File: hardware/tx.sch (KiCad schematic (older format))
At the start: 63 parts, among them Q1 RE1C002UN, U1 ADF4158, U10 HMC431LP4, U12 PAT1220-6dB, U15 SMA, U17 SE5004L, U3 PAT1220-6dB, U7 TLV172DCK

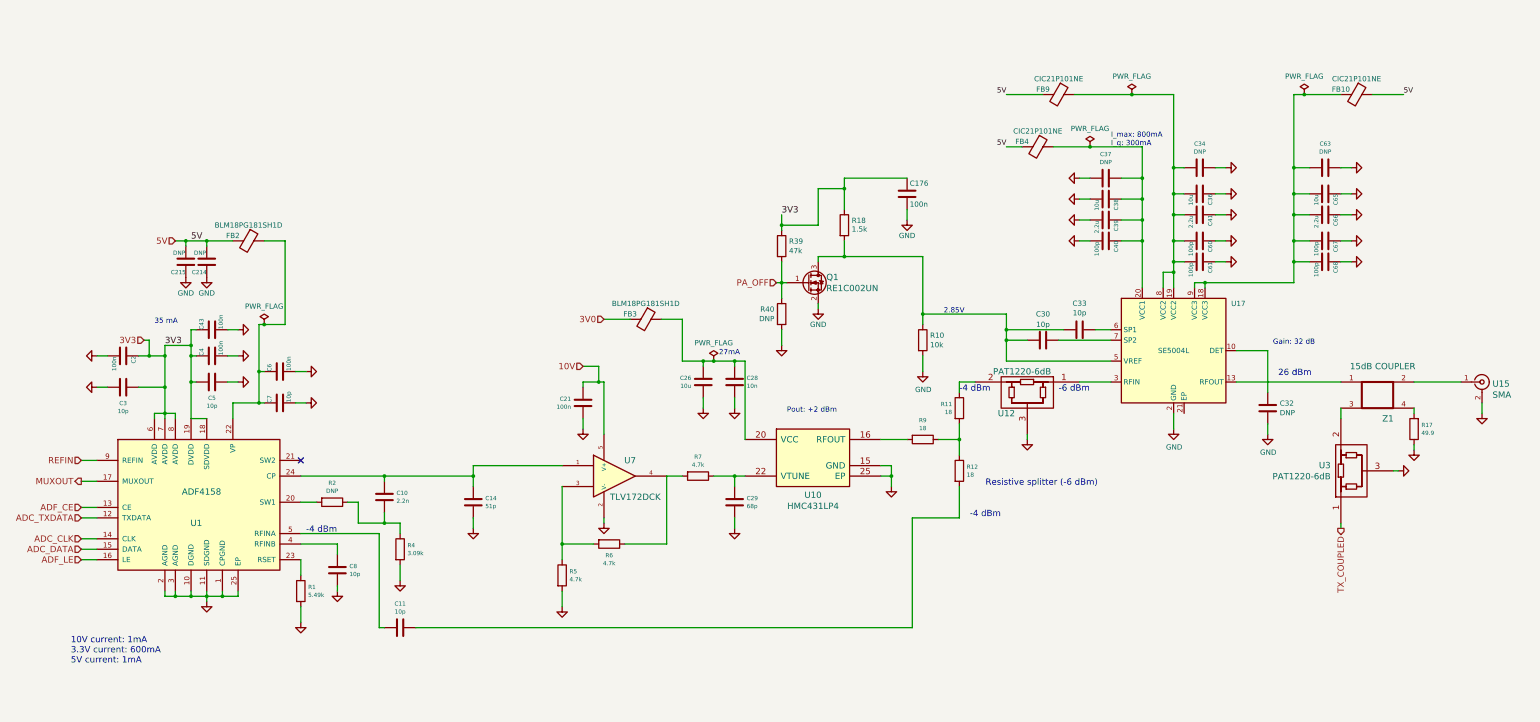
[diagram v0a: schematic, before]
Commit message: Improved tx sheet and corresponding documentation.
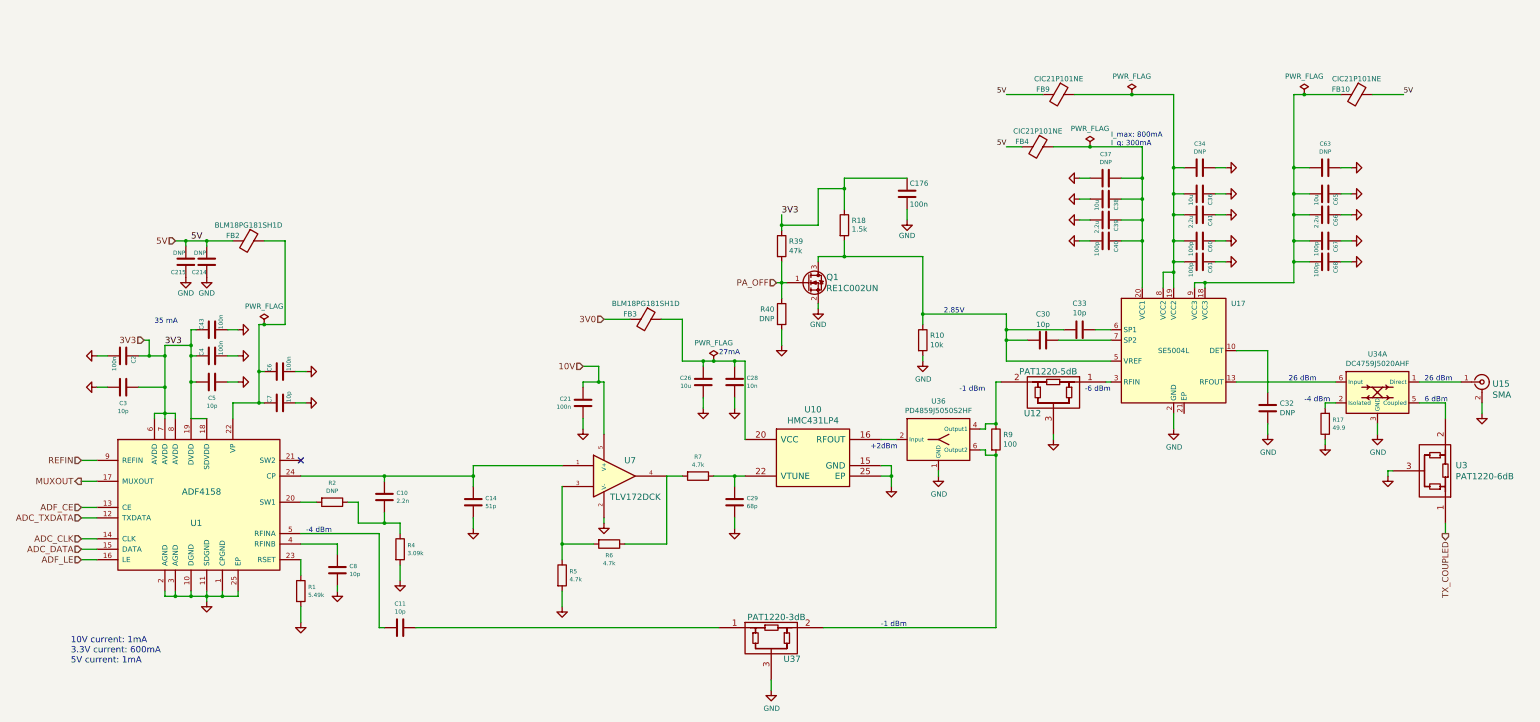
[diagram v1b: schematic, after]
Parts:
- removed R11, R12: 18, Resistor_SMD:R_0402_1005Metric, symbol Device:R
- removed Z1: 15dB COUPLER, fmcw:coupler, symbol fmcw-rescue:BRANCHLINE-fmcw3-rescue
- added U34: DC4759J5020AHF, RF_Converter:Anaren_Coupler_DC4759J5020AHF, symbol RF:DC4759J5020AHF
- added U36: PD4859J5050S2HF, RF_Converter:Anaren_0805_2012Metric-6, symbol RF:PD4859J5050S2HF
- added U37: PAT1220-3dB, fmcw:PAT1220, symbol fmcw-rescue:PAT1220-fmcw3-rescue
- R9: value 18 -> 100; footprint Resistor_SMD:R_0402_1005Metric -> Resistor_SMD:R_0603_1608Metric; MFN ERJ-2RKF18R0X -> ERA-3AEB101V
- U12: value PAT1220-6dB -> PAT1220-5dB; MFN PAT1220-C-6DB-T5 -> PAT1220-C-5DB-T5
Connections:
- net GND: now also U34.3 (GND), U34.4 (GND), U36.1 (GND), U36.3 (GND), U36.5 (GND), U37.3
- net at U10.16 (RFOUT): now also U36.2 (Input); no longer R9.2
- net at U15.1 (In): now also U34.1 (Direct)
- net at R9.1: now also U12.2, U36.4 (Output1)
- net at C11.1: now also U37.1
- net at U3.2: now also U34.5 (Coupled)
- net at U17.13 (RFOUT): now also U34.6 (Input)
- net at R17.2: now also U34.2 (Isolated)
- new net: R9.2, U36.6 (Output2), U37.2
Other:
- note added: "+2dBm"
- note added: "-1 dBm"
- note added: "6 dBm"
- note removed: "Gain: 32 dB"
- note removed: "Pout: +2 dBm"
- note removed: "Resistive splitter (-6 dBm)"
- moved on the sheet: R17, U12, U3

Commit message: Improved documentation and parts of the schematic.
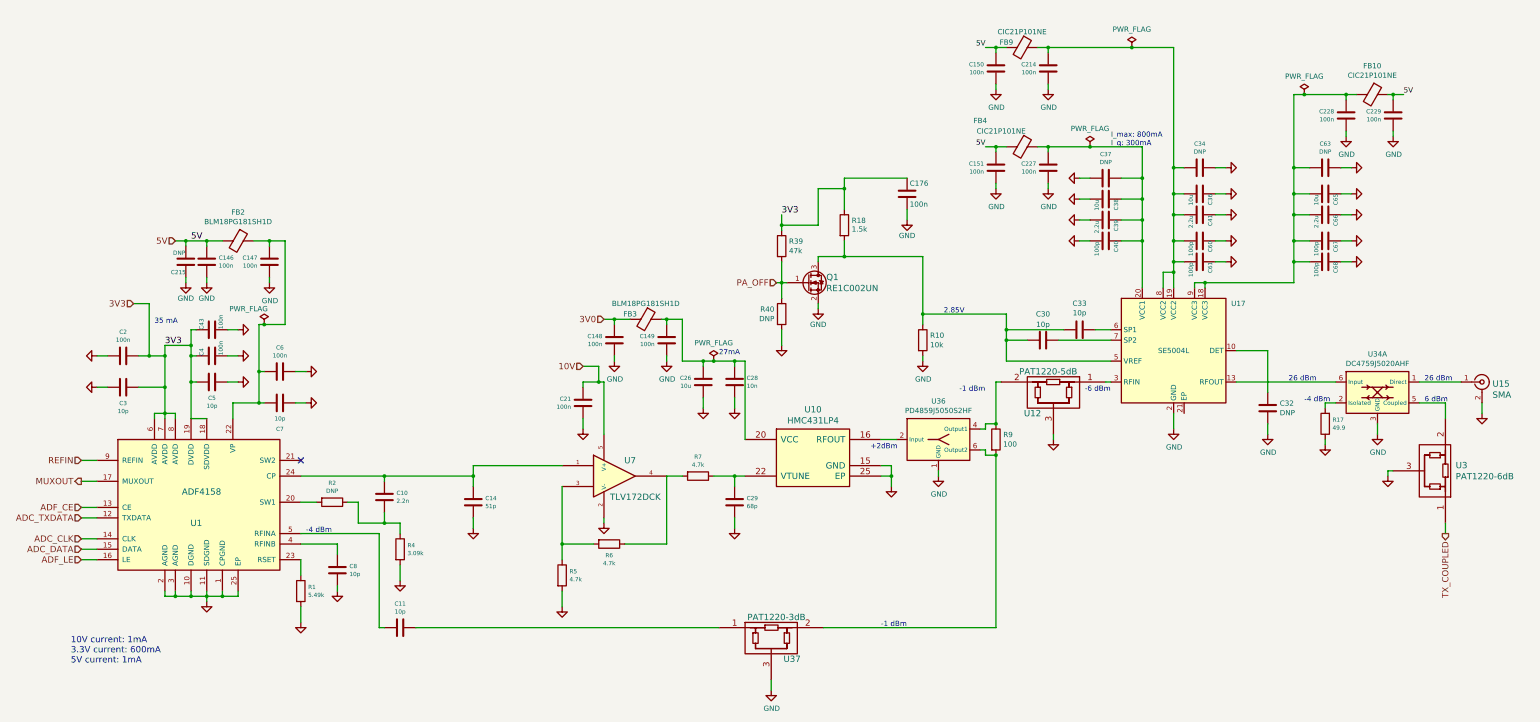
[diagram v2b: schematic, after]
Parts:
- added C146, C147, C148, C149, C150, C151, C227, C228, C229: 100n, Capacitor_SMD:C_0402_1005Metric, symbol Device:C
- C214: value DNP -> 100n; footprint Capacitor_SMD:C_0805_2012Metric -> Capacitor_SMD:C_0402_1005Metric; MFN (none) -> CL05B104KO5NNNC
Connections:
- net 3V0: now also C148.1
- net 5V: now also C146.1, C150.1, C151.1, C229.1; no longer C214.2
- net GND: now also C214.2, C146.2, C147.2, C148.2, C149.2, C150.2, C151.2, C227.2, C228.2, C229.2; no longer C214.1
- net at C26.1, C28.1, FB3.1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: now also C149.1
- net at C6.1, C7.1, FB2.1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: now also C147.1
- net at C37.1, C38.1, C39.1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: now also C227.1
- net at C63.2, C65.2, C66.2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: now also C228.1
- net at C34.2, C36.2, C41.2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: now also C214.1
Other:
- moved on the sheet: FB10, FB2, FB4, FB9

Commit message: Changed components to official libs.
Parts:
- removed C215: DNP, Capacitor_SMD:C_0805_2012Metric, symbol Device:C
- U1: footprint Package_DFN_QFN:WQFN-24-1EP_4x4mm_P0.5mm_EP2.7x2.7mm -> Package_CSP:LFCSP-24-1EP_4x4mm_P0.5mm_EP2.5x2.5mm; symbol fmcw-rescue:ADF4158-fmcw3-rescue -> Timer_PLL:ADF4158
- U10: footprint Package_DFN_QFN:VQFN-24-1EP_4x4mm_P0.5mm_EP2.45x2.45mm -> Package_DFN_QFN:QFN-24-1EP_4x4mm_P0.5mm_EP2.8x2.8mm; symbol fmcw-rescue:HMC431LP4-fmcw3-rescue -> RF:HMC431
- U12: footprint fmcw:PAT1220 -> RF_Converter:RF_Attenuator_Susumu_PAT1220; symbol fmcw-rescue:PAT1220-fmcw3-rescue -> RF:PAT1220x5DB
- U3: footprint fmcw:PAT1220 -> RF_Converter:RF_Attenuator_Susumu_PAT1220; symbol fmcw-rescue:PAT1220-fmcw3-rescue -> RF:PAT1220x6DB
- U37: footprint fmcw:PAT1220 -> RF_Converter:RF_Attenuator_Susumu_PAT1220; symbol fmcw-rescue:PAT1220-fmcw3-rescue -> RF:PAT1220x3DB
- U7: symbol fmcw-rescue:TLV172DCK-fmcw3-rescue -> Amplifier_Operational:TLV172IDCK
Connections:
- net GND: now also R4.1; no longer R4.2
- net at C10.2, R2.1: now also R4.2; no longer R4.1
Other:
- moved on the sheet: C10, C14, C146, C147, C2, C3, C4, C43, C5, C6, C7, C8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

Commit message: Finished design, began routing.
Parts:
- added C251, C252: 10p, Capacitor_SMD:C_0402_1005Metric, symbol Device:C
- C110: renamed from C10; MFN CL05B223KP5NNNC -> CL05B222KB5VPNC
- R40: renamed from R5; MFN ERJ-2GEJ472X -> ERJ-2GEJ472X
- R41: renamed from R6; MFN ERJ-2GEJ472X -> ERJ-2GEJ472X
- R42: renamed from R7; MFN ERJ-2GEJ472X -> ERJ-2GEJ472X
- U19: renamed from U34; footprint RF_Converter:Anaren_Coupler_DC4759J5020AHF -> RF_Converter:Anaren_0805_2012Metric-6; symbol RF:DC4759J5020AHF -> RF:DC4759J5020AHF-2
- renumbered C2 to C102, C3 to C103, C43 to C104, C4 to C105, C5 to C106, C8 to C107, C6 to C108, C7 to C109, C147 to C111, C11 to C112, C146 to C113, C14 to C114, C21 to C115, C148 to C116, C149 to C117, C26 to C118, C28 to C119, C29 to C120, C176 to C121, C150 to C122, C151 to C123, C30 to C124, C214 to C125, C227 to C126, C33 to C127, C37 to C128, C38 to C129, C39 to C130, C40 to C131, C34 to C132, C36 to C133, C41 to C134, C60 to C135, C61 to C136, C32 to C137, C63 to C138, C65 to C139, C66 to C140, C67 to C141, C68 to C142, C228 to C143, C229 to C144, FB2 to FB6, FB3 to FB7, FB9 to FB8, FB4 to FB9, U15 to J3, Q1 to Q2, R1 to R37, R2 to R38, R4 to R39, R39 to R43, R40 to R44, R18 to R45, R10 to R46, R9 to R47, R17 to R48, U1 to U12, U7 to U13, U37 to U14, U10 to U15, U36 to U16, U12 to U17, U17 to U18, U3 to U20
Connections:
- net at J3.1 (In): now also U19.6 (Direct); no longer U19.1 (Direct)
- net at U17.1: now also C251.2; no longer U18.3 (RFIN)
- net at U20.2: now also U19.2 (Coupled); no longer U19.5 (Coupled)
- net at R48.2: now also U19.5 (Isolated); no longer U19.2 (Isolated)
- net at U18.13 (RFOUT): now also C252.2; no longer U19.6 (Input)
- new net: C251.1, U18.3 (RFIN)
- new net: C252.1, U19.1 (Input)
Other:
- moved on the sheet: C122, C123, C125, C126, C128, C129, C130, C131, C132, C133, C134, C135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

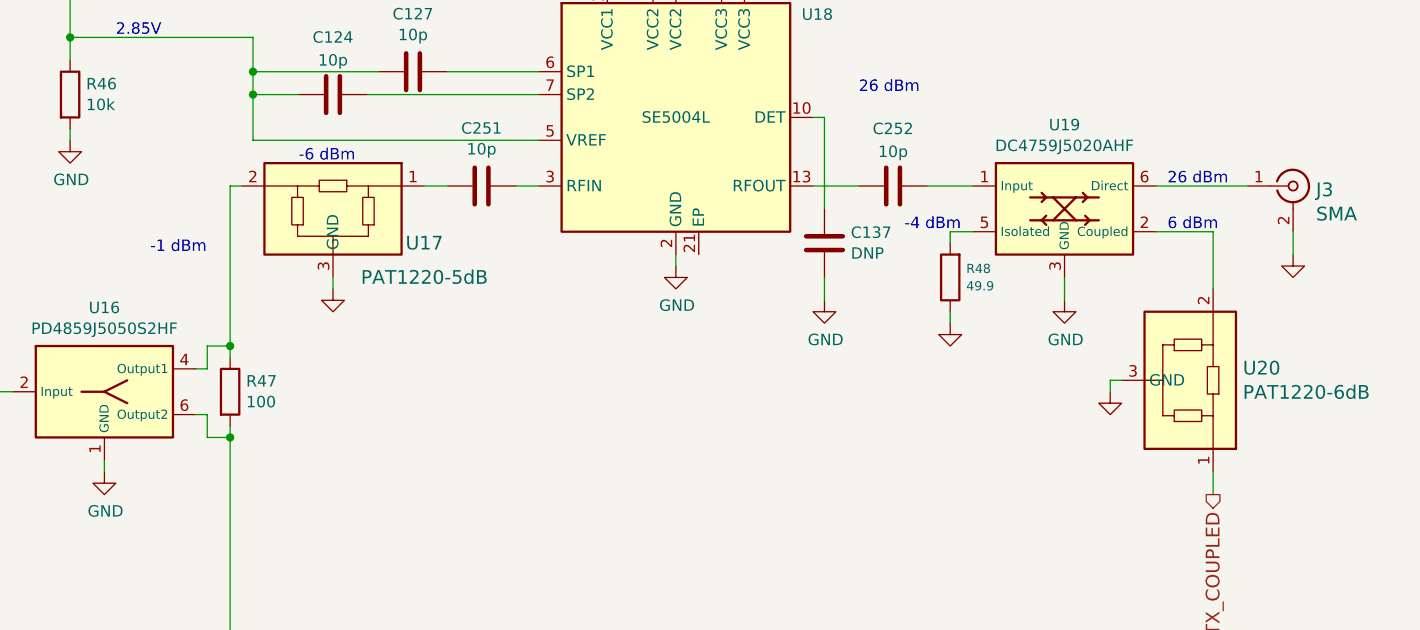
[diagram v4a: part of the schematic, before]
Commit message: Placed most major components.
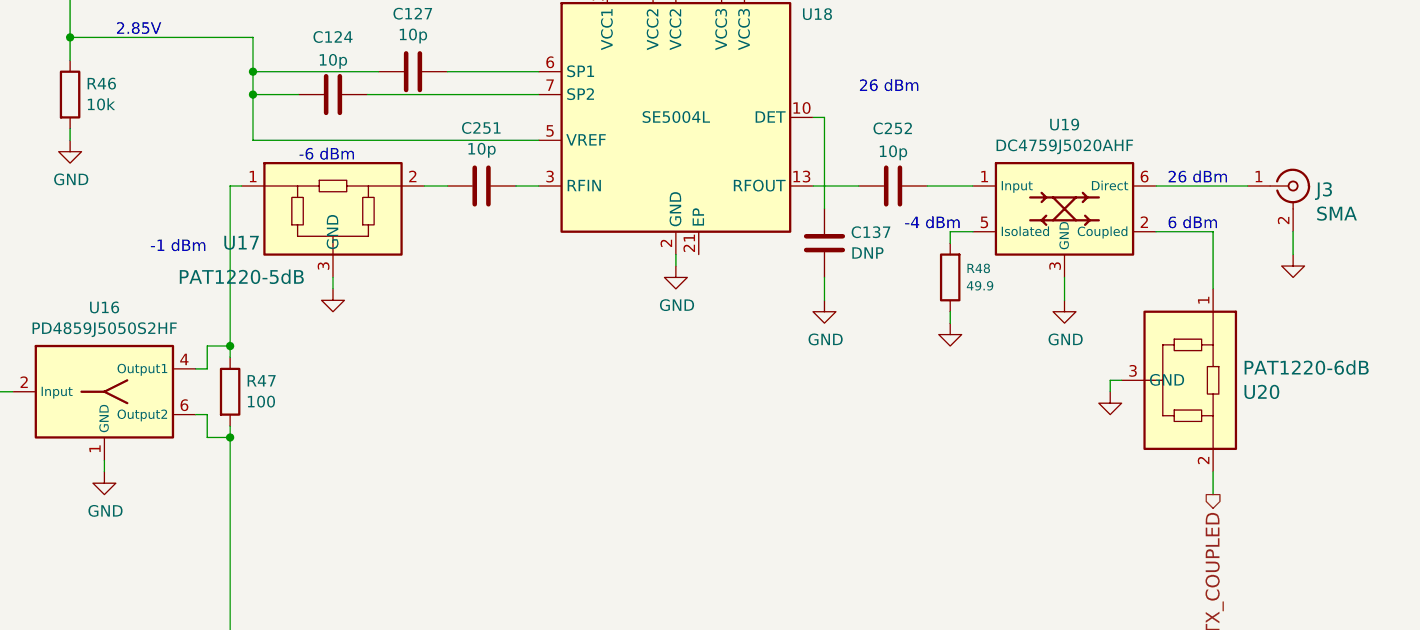
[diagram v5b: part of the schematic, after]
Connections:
- net TX_COUPLED: now also U20.2; no longer U20.1
- net at U17.1: now also R47.1, U16.4 (Output1); no longer C251.2
- net at U19.2 (Coupled): now also U20.1; no longer U20.2
- new net: C251.2, U17.2
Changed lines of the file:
@@
 F 4 "PAT1220-C-5DB-T5" H 150 100 50  0001 C CNN "MFN"
 	1    11350 5100
-	-1   0    0    -1
+	1    0    0    -1
 $EndComp
 $Comp
@@
 F 4 "PAT1220-C-6DB-T5" H 900 0   50  0001 C CNN "MFN"
 	1    15100 5850
-	0    1    -1   0
-$EndComp
-$Comp
+	0    1    1    0
+$EndComp
+$Comp

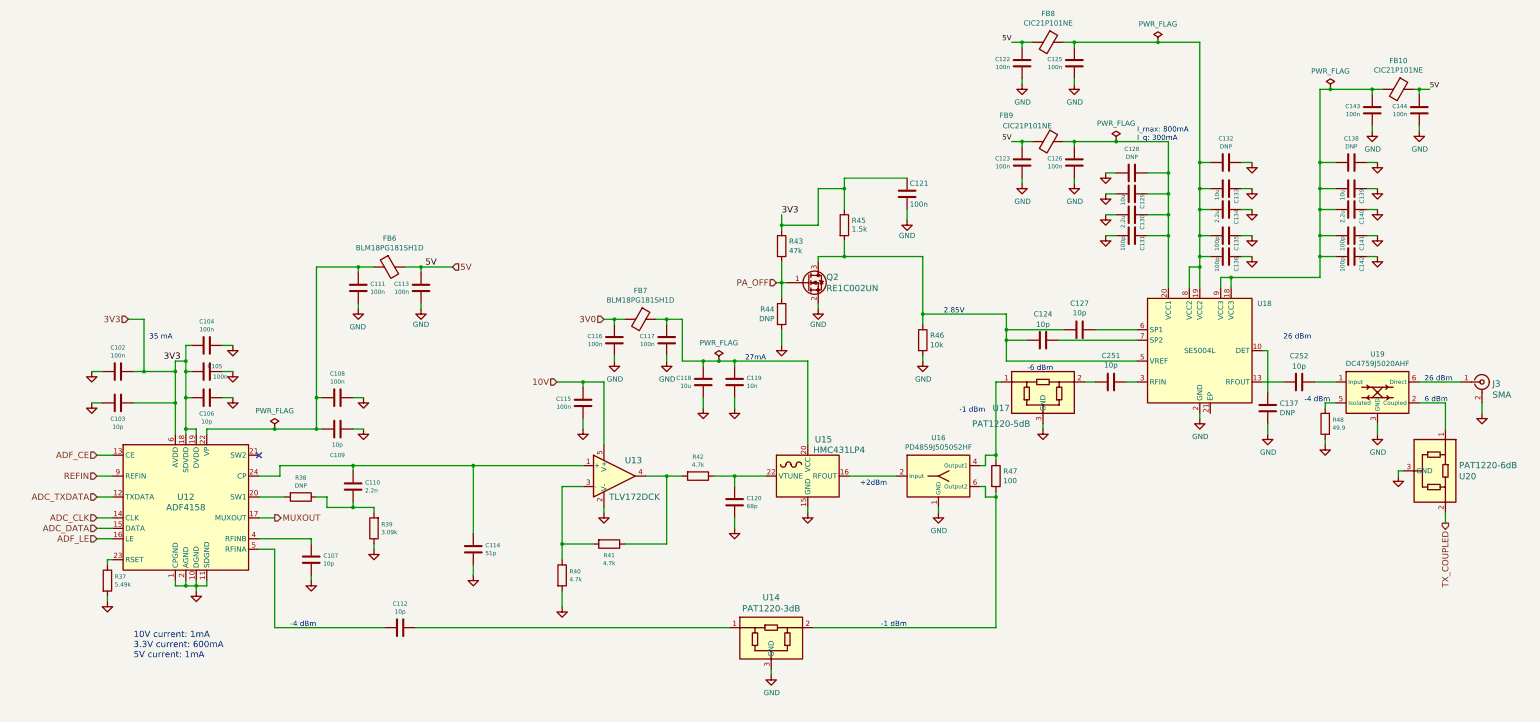
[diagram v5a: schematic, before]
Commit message: Completed clock placement and routing.
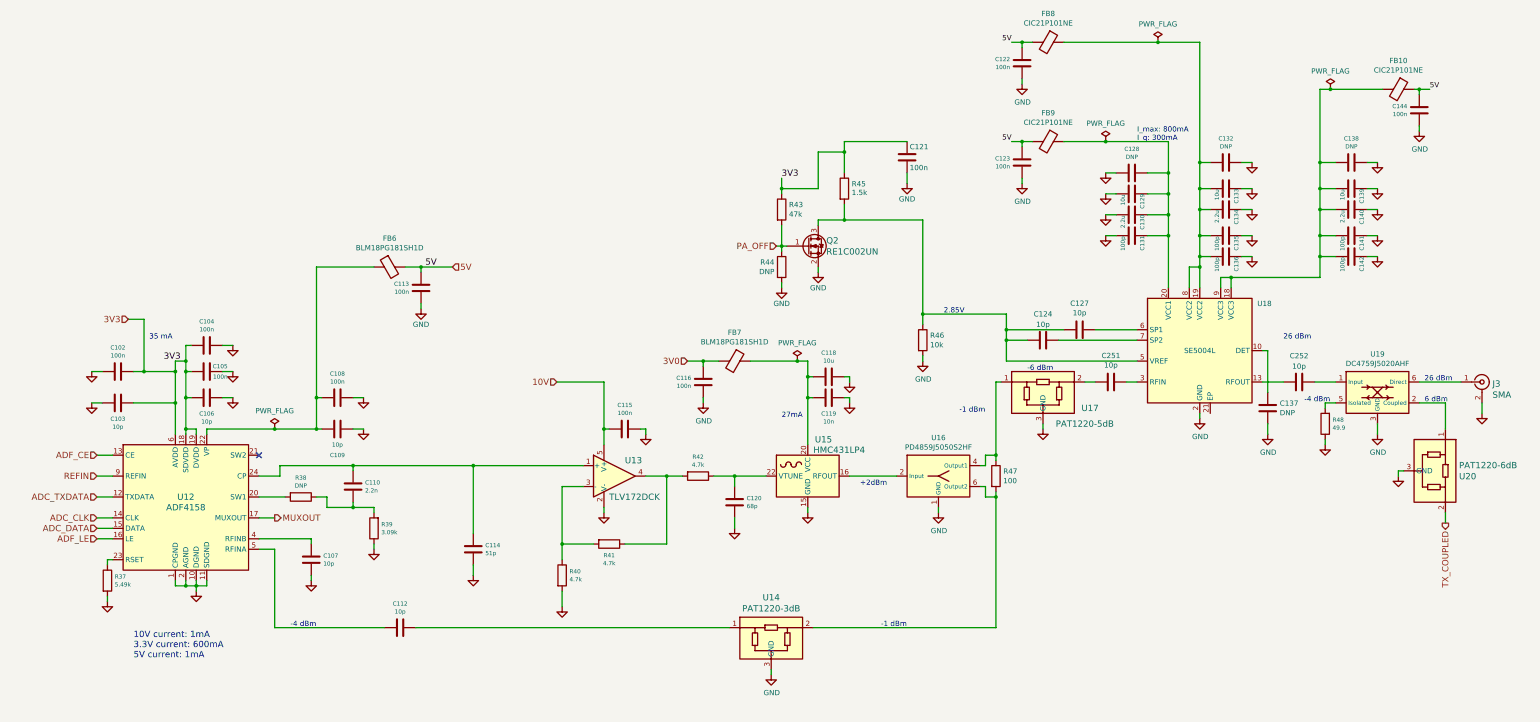
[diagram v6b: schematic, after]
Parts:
- removed C111, C117, C125, C126, C143: 100n, Capacitor_SMD:C_0402_1005Metric, symbol Device:C
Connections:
- net 10V: now also C115.2; no longer C115.1
- net GND: now also C115.1, C118.1, C119.1; no longer C115.2, C118.2, C119.2
- net at FB7.1, U15.20 (VCC): now also C118.2, C119.2; no longer C118.1, C119.1
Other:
- moved on the sheet: C115, C116, C118, C119, C121, FB7, Q2, R43, R44, R45

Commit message: Better MFNs for RF DC blocking caps.
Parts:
- C112, C124, C127, C251, C252: MFN GRM1555C1H100FA01D -> 500R07S100JV4T
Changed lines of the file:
@@
 F 2 "Capacitor_SMD:C_0402_1005Metric" H 5238 7200 30  0001 C CNN
 F 3 "" H 5200 7350 60  0000 C CNN
-F 4 "GRM1555C1H100FA01D" H 0   0   50  0001 C CNN "MFN"
+F 4 "500R07S100JV4T" H 0   0   50  0001 C CNN "MFN"
 	1    5200 7350
 	0    1    1    0
@@
 F 2 "Capacitor_SMD:C_0402_1005Metric" H 11388 4450 50  0001 C CNN
 F 3 "~" H 11350 4600 50  0001 C CNN
-F 4 "GRM1555C1H100FA01D" H 0   0   50  0001 C CNN "MFN"
+F 4 "500R07S100JV4T" H 0   0   50  0001 C CNN "MFN"
 	1    11350 4600
 	0    1    1    0
@@
 F 2 "Capacitor_SMD:C_0402_1005Metric" H 11738 4350 50  0001 C CNN
 F 3 "~" H 11700 4500 50  0001 C CNN
-F 4 "GRM1555C1H100FA01D" H 0   0   50  0001 C CNN "MFN"
+F 4 "500R07S100JV4T" H 0   0   50  0001 C CNN "MFN"
 	1    11700 4500
 	0    1    1    0
@@
 F 2 "Capacitor_SMD:C_0402_1005Metric" H 12038 4850 50  0001 C CNN
 F 3 "~" H 12000 5000 50  0001 C CNN
-F 4 "GRM1555C1H100FA01D" H 300 500 50  0001 C CNN "MFN"
+F 4 "500R07S100JV4T" H 300 500 50  0001 C CNN "MFN"
 	1    12000 5000
 	0    1    1    0
@@
 F 2 "Capacitor_SMD:C_0402_1005Metric" H 13838 4850 50  0001 C CNN
 F 3 "~" H 13800 5000 50  0001 C CNN
-F 4 "GRM1555C1H100FA01D" H 2450 400 50  0001 C CNN "MFN"
+F 4 "500R07S100JV4T" H 2450 400 50  0001 C CNN "MFN"
 	1    13800 5000
 	0    1    1    0
